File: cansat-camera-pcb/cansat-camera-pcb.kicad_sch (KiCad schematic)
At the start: 25 parts, among them SW2 SW_Push, U4 STM32H743ZITx, Y1 24MHz

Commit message: USB fix
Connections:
- net usb_dm: now reaches U4.75 (PB14)
- net usb_dp: now reaches U4.76 (PB15)
- no-connect marks 45 -> 43
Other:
- sheet Connector section ports: added USB_DM, USB_DP; removed none
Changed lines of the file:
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@@
 	)
 	(no_connect
-		(at 123.19 148.59)
-	)
-	(no_connect
 		(at 123.19 123.19)
 	)
@@
 	)
 	(no_connect
-		(at 123.19 151.13)
-	)
-	(no_connect
 		(at 57.15 128.27)
 	)
@@
 	(wire
 		(pts
+			(xy 157.48 212.09) (xy 158.75 212.09)
+		)
+		(stroke
+			(width 0)
+			(type default)
+		)
+	)
+	(wire
+		(pts
 			(xy 74.93 57.15) (xy 77.47 57.15)
 		)
@@
 	(wire
 		(pts
+			(xy 157.48 207.01) (xy 158.75 207.01)
+		)
+		(stroke
+			(width 0)
+			(type default)
+		)
+	)
+	(wire
+		(pts
 			(xy 45.72 226.06) (xy 46.99 226.06)
 		)
@@
 	(wire
 		(pts
+			(xy 157.48 209.55) (xy 158.75 209.55)
+		)
+		(stroke
+			(width 0)
+			(type default)
+		)
+	)
+	(wire
+		(pts
 			(xy 43.18 260.35) (xy 53.34 260.35)
 		)
@@
 	(wire
 		(pts
-			(xy 157.48 209.55) (xy 158.75 209.55)
-		)
-		(stroke
-			(width 0)
-			(type default)
-		)
-	)
-	(wire
-		(pts
 			(xy 158.75 135.89) (xy 160.02 135.89)
 		)
@@
 	(wire
 		(pts
-			(xy 157.48 207.01) (xy 158.75 207.01)
+			(xy 157.48 204.47) (xy 158.75 204.47)
 		)
 		(stroke
@@
 		)
 	)
+	(label "usb_dm"
+		(at 157.48 212.09 180)
+		(effects
+			(font
+				(size 1.27 1.27)
+			)
+			(justify right bottom)
+		)
+	)
 	(label "VREF_PIN"
 		(at 55.88 80.01 180)
@@
 		)
 	)
+	(label "usb_dp"
+		(at 157.48 209.55 180)
+		(effects
+			(font
+				(size 1.27 1.27)
+			)
+			(justify right bottom)
+		)
+	)
+	(label "usb_dp"
+		(at 123.19 151.13 0)
+		(effects
+			(font
+				(size 1.27 1.27)
+			)
+			(justify left bottom)
+		)
+	)
 	(label "FMC_SDCKE0"
 		(at 124.46 163.83 0)
@@
 	)
 	(label "UART4_RX"
-		(at 157.48 209.55 180)
+		(at 157.48 207.01 180)
 		(effects
 			(font
@@
 		)
 	)
+	(label "usb_dm"
+		(at 123.19 148.59 0)
+		(effects
+			(font
+				(size 1.27 1.27)
+			)
+			(justify left bottom)
+		)
+	)
 	(label "FMC_D3"
 		(at 158.75 53.34 180)
@@
 	)
 	(label "UART4_TX"
-		(at 157.48 207.01 180)
+		(at 157.48 204.47 180)
 		(effects
 			(font
@@
 			)
 		)
-		(pin "OBC_UART_Rx" input
-			(at 158.75 209.55 180)
-			(effects
-				(font
-					(size 1.27 1.27)
-				)
-				(justify left)
-			)
-		)
 		(pin "BOOT0" input
 			(at 190.5 205.74 0)
@@
 		)
 		(pin "OBC_UART_Tx" output
+			(at 158.75 204.47 180)
+			(effects
+				(font
+					(size 1.27 1.27)
+				)
+				(justify left)
+			)
+		)
+		(pin "USB_DP" bidirectional
+			(at 158.75 209.55 180)
+			(effects
+				(font
+					(size 1.27 1.27)
+				)
+				(justify left)
+			)
+		)
+		(pin "USB_DM" bidirectional
+			(at 158.75 212.09 180)
+			(effects
+				(font
+					(size 1.27 1.27)
+				)
+				(justify left)
+			)
+		)
+		(pin "OBC_UART_Rx" input
 			(at 158.75 207.01 180)
 			(effects

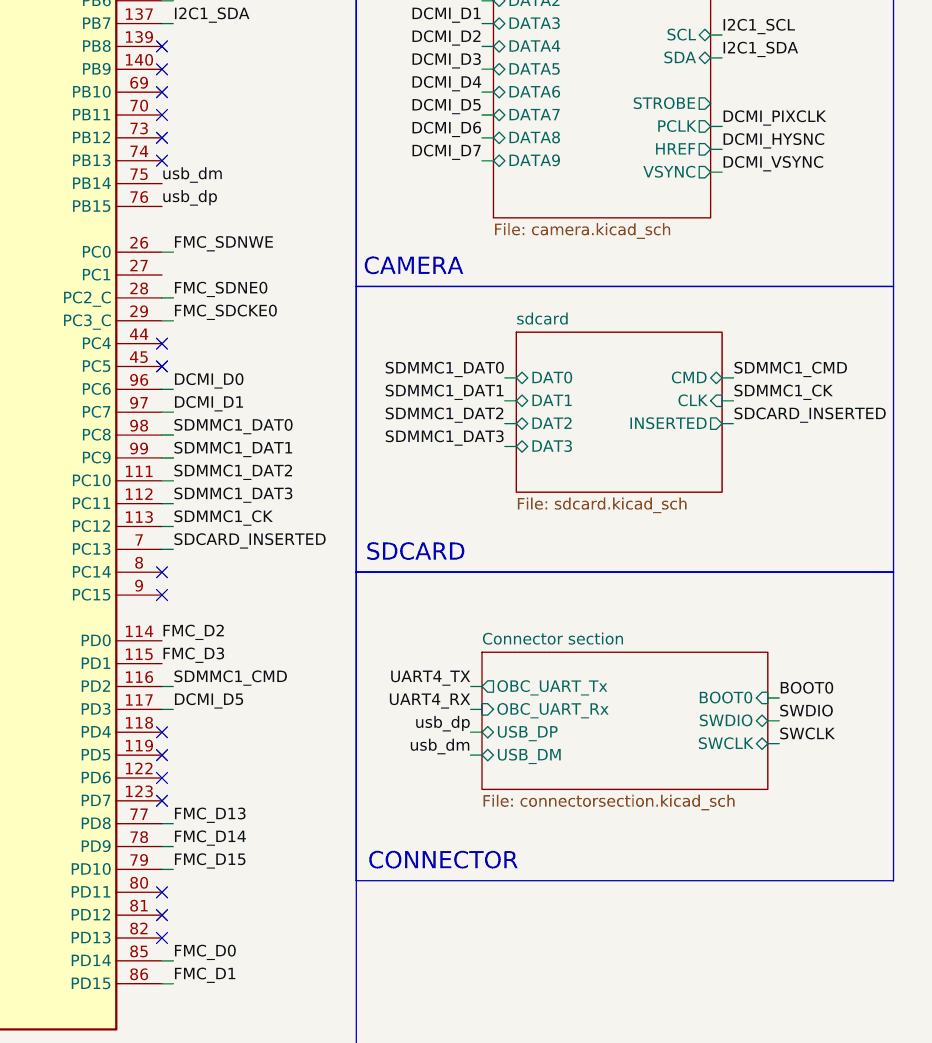
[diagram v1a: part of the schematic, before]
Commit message: sdcard deleted form this PCB
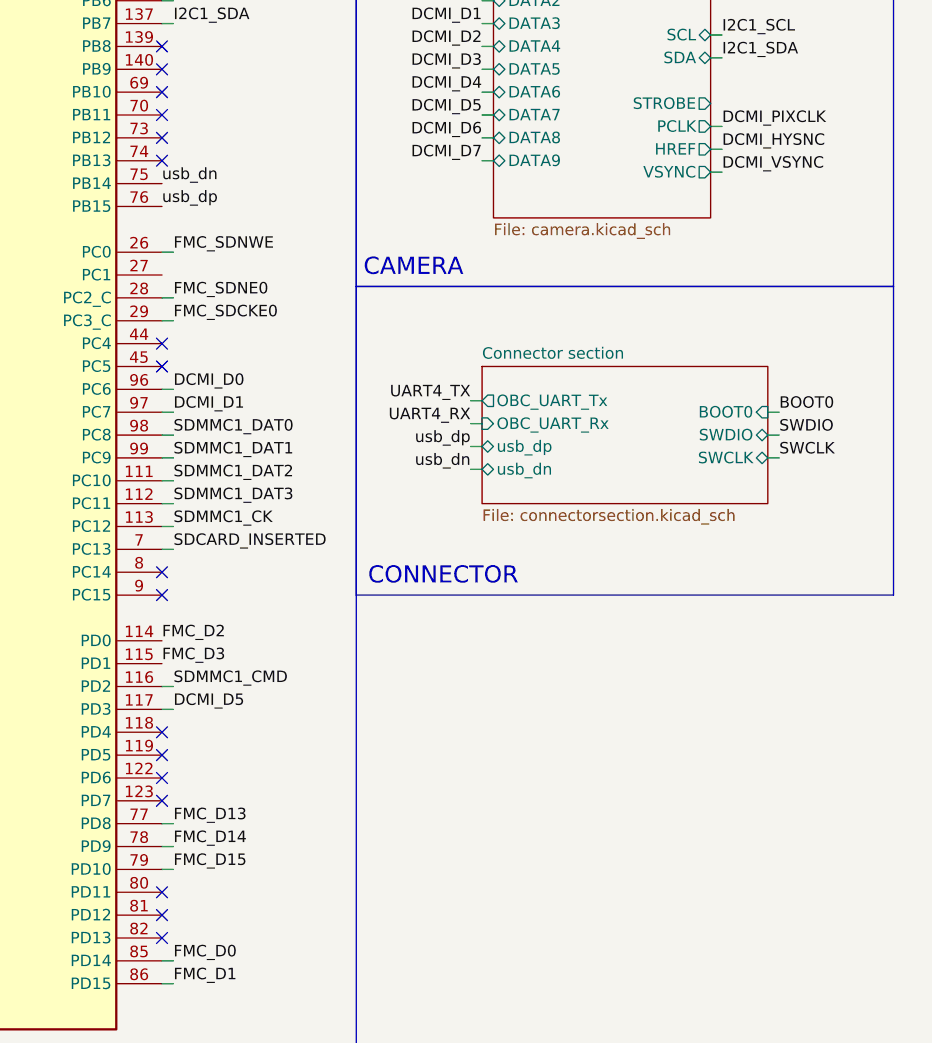
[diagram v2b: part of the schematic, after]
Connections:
- net usb_dm renamed usb_dn
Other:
- removed sheet sdcard
- sheet Connector section ports: added usb_dn, usb_dp; removed USB_DM, USB_DP
- note removed: "SDCARD"

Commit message: -
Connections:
- net usb_dn renamed usb_DN
- net usb_dp renamed usb_DP
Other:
- sheet Connector section ports: added usb_DN, usb_DP; removed usb_dn, usb_dp
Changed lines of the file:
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@@
 		)
 	)
-	(label "usb_dn"
+	(label "usb_DN"
 		(at 157.48 180.34 180)
 		(effects
@@
 		)
 	)
-	(label "usb_dp"
+	(label "usb_DP"
 		(at 157.48 177.8 180)
 		(effects
@@
 		)
 	)
-	(label "usb_dp"
+	(label "usb_DP"
 		(at 123.19 151.13 0)
 		(effects
@@
 		)
 	)
-	(label "usb_dn"
+	(label "usb_DN"
 		(at 123.19 148.59 0)
 		(effects
@@
 			)
 		)
-		(pin "usb_dn" bidirectional
+		(pin "usb_DN" bidirectional
 			(at 158.75 180.34 180)
 			(effects
@@
 			)
 		)
-		(pin "usb_dp" bidirectional
+		(pin "usb_DP" bidirectional
 			(at 158.75 177.8 180)
 			(effects

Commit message: fixes
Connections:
- net LTE_reset: now reaches U4.1 (PE2)
- net LTE_pwrkey: now reaches U4.2 (PE3)
- no-connect marks 43 -> 41
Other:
- sheet Connector section ports: added pwrkey, reset; removed none
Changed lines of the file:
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@@
 	)
 	(no_connect
-		(at 57.15 189.23)
-	)
-	(no_connect
 		(at 57.15 115.57)
 	)
@@
 	)
 	(no_connect
-		(at 57.15 191.77)
-	)
-	(no_connect
 		(at 123.19 125.73)
 	)
@@
 	(wire
 		(pts
-			(xy 191.77 173.99) (xy 190.5 173.99)
+			(xy 191.77 171.45) (xy 190.5 171.45)
 		)
 		(stroke
@@
 	(wire
 		(pts
-			(xy 190.5 176.53) (xy 191.77 176.53)
+			(xy 190.5 173.99) (xy 191.77 173.99)
 		)
 		(stroke
@@
 	(wire
 		(pts
+			(xy 55.88 191.77) (xy 57.15 191.77)
+		)
+		(stroke
+			(width 0)
+			(type default)
+		)
+	)
+	(wire
+		(pts
 			(xy 55.88 219.71) (xy 57.15 219.71)
 		)
@@
 	(wire
 		(pts
-			(xy 190.5 179.07) (xy 191.77 179.07)
+			(xy 55.88 189.23) (xy 57.15 189.23)
+		)
+		(stroke
+			(width 0)
+			(type default)
+		)
+	)
+	(wire
+		(pts
+			(xy 190.5 176.53) (xy 191.77 176.53)
 		)
 		(stroke
@@
 	(wire
 		(pts
+			(xy 190.5 179.07) (xy 191.77 179.07)
+		)
+		(stroke
+			(width 0)
+			(type default)
+		)
+	)
+	(wire
+		(pts
 			(xy 184.15 99.06) (xy 185.42 99.06)
 		)
@@
 	(wire
 		(pts
+			(xy 190.5 181.61) (xy 191.77 181.61)
+		)
+		(stroke
+			(width 0)
+			(type default)
+		)
+	)
+	(wire
+		(pts
 			(xy 49.53 67.31) (xy 46.99 67.31)
 		)
@@
 		)
 	)
+	(label "LTE_reset"
+		(at 191.77 179.07 0)
+		(effects
+			(font
+				(size 1.27 1.27)
+			)
+			(justify left bottom)
+		)
+	)
 	(label "VREF_PIN"
 		(at 55.88 80.01 180)
@@
 		)
 	)
+	(label "LTE_pwrkey"
+		(at 55.88 191.77 180)
+		(effects
+			(font
+				(size 1.27 1.27)
+			)
+			(justify right bottom)
+		)
+	)
 	(label "FMC_A6"
 		(at 55.88 171.45 180)
@@
 	)
 	(label "BOOT0"
-		(at 191.77 173.99 0)
+		(at 191.77 171.45 0)
 		(effects
 			(font
@@
 		)
 	)
+	(label "LTE_pwrkey"
+		(at 191.77 181.61 0)
+		(effects
+			(font
+				(size 1.27 1.27)
+			)
+			(justify left bottom)
+		)
+	)
 	(label "VDDA_PIN"
 		(at 107.95 55.88 90)
@@
 	)
 	(label "SWCLK"
-		(at 191.77 179.07 0)
+		(at 191.77 176.53 0)
 		(effects
 			(font
@@
 		)
 	)
+	(label "LTE_reset"
+		(at 55.88 189.23 180)
+		(effects
+			(font
+				(size 1.27 1.27)
+			)
+			(justify right bottom)
+		)
+	)
 	(label "SWDIO"
-		(at 191.77 176.53 0)
+		(at 191.77 173.99 0)
 		(effects
 			(font
@@
 		)
 		(pin "BOOT0" input
-			(at 190.5 173.99 0)
+			(at 190.5 171.45 0)
 			(effects
 				(font
@@
 		)
 		(pin "SWDIO" bidirectional
-			(at 190.5 176.53 0)
+			(at 190.5 173.99 0)
 			(effects
 				(font
@@
 		)
 		(pin "SWCLK" bidirectional
-			(at 190.5 179.07 0)
+			(at 190.5 176.53 0)
 			(effects
 				(font
@@
 			)
 		)
+		(pin "reset" output
+			(at 190.5 179.07 0)
+			(effects
+				(font
+					(size 1.27 1.27)
+				)
+				(justify right)
+			)
+		)
+		(pin "pwrkey" output
+			(at 190.5 181.61 0)
+			(effects
+				(font
+					(size 1.27 1.27)
+				)
+				(justify right)
+			)
+		)

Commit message: Sdram finish, cleanup
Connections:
- net FMC_A12: now reaches U4.87 (PG2)
- net FMC_AP: no longer names the net of U4.18 (PF6)
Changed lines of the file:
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@@
 	)
 	(no_connect
-		(at 57.15 102.87)
-	)
-	(no_connect
 		(at 123.19 82.55)
 	)
@@
 	)
 	(no_connect
+		(at 57.15 156.21)
+	)
+	(no_connect
 		(at 123.19 191.77)
 	)
@@
 	(wire
 		(pts
+			(xy 55.88 102.87) (xy 57.15 102.87)
+		)
+		(stroke
+			(width 0)
+			(type default)
+		)
+	)
+	(wire
+		(pts
 			(xy 39.37 228.6) (xy 39.37 231.14)
 		)
@@
 		)
 	)
+	(label "FMC_A12"
+		(at 55.88 102.87 180)
+		(effects
+			(font
+				(size 1.27 1.27)
+			)
+			(justify right bottom)
+		)
+	)
 	(label "USART2_TX"
 		(at 124.46 74.93 0)
@@
 		)
 	)
-	(label "FMC_A10"
+	(label "FMC_A11"
 		(at 185.42 73.66 0)
 		(effects
@@
 		)
 	)
-	(label "FMC_AP"
+	(label "FMC_A10"
 		(at 185.42 71.12 0)
 		(effects
@@
 		)
 	)
-	(label "FMC_A11"
+	(label "FMC_A12"
 		(at 185.42 76.2 0)
 		(effects
@@
 		)
 	)
-	(label "FMC_AP"
-		(at 57.15 156.21 180)
-		(effects
-			(font
-				(size 1.27 1.27)
-			)
-			(justify right bottom)
-		)
-	)

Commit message: Camera_Final
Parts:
- removed Y1: 24MHz, Crystal:Crystal_SMD_3225-4Pin_3.2x2.5mm, symbol Device:Crystal_Small
- added Y1: 24MHz, Crystal:Crystal_SMD_3225-4Pin_3.2x2.5mm, symbol Device:Crystal_GND24_Small
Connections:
- net GND: now also Y1.2, Y1.4
- net at C1.1, U4.23 (PH0): now also Y1.3
- net at C34.2, U4.24 (PH1): now also Y1.1
- net I2C2_SCL: now reaches U4.69 (PB10)
- net I2C2_SDA: now reaches U4.70 (PB11)
- net I2C4_SCL: now reaches U4.81 (PD12)
- net I2C4_SDA: now reaches U4.82 (PD13)
- net SDCARD_INSERTED: no longer names the net of U4.7 (PC13)
- net SDMMC1_CK: no longer names the net of U4.113 (PC12)
- net SDMMC1_DAT0: no longer names the net of U4.98 (PC8)
- net SDMMC1_DAT1: no longer names the net of U4.99 (PC9)
- net SDMMC1_DAT2: no longer names the net of U4.111 (PC10)
- net SDMMC1_DAT3: no longer names the net of U4.112 (PC11)
- no-connect marks 41 -> 44
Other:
- added sheet sz4pF4SZ (extraf4sz.kicad_sch)
- sheet Connector section ports: added I2C2_SCL, I2C2_SDA, I2C4_SCL, I2C4_SDA; removed none
- note added: "Extra"

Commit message: Camera_Final
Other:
- removed sheet sz4pF4SZ
- note removed: "Extra"
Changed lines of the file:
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@@
 	)
 	(rectangle
-		(start 144.78 194.31)
-		(end 204.47 228.6)
-		(stroke
-			(width 0)
-			(type default)
-		)
-		(fill
-			(type none)
-		)
-	)
-	(rectangle
 		(start 19.05 17.78)
 		(end 144.78 281.94)
@@
 		)
 	)
-	(text "Extra"
-		(exclude_from_sim no)
-		(at 149.098 226.822 0)
-		(effects
-			(font
-				(size 1.905 1.905)
-			)
-		)
-	)
 	(junction
 		(at 100.33 57.15)
@@
 			)
 		)
-		(instances
-			(project "cansat-camera-pcb"
-				(path "/ff55e53a-9379-43eb-9b08-9bace1f81889"
-					(page "6")
-				)
-			)
-		)
-	)
-	(sheet
-		(at 161.29 203.2)
-		(size 21.59 13.97)
-		(exclude_from_sim no)
-		(in_bom yes)
-		(on_board yes)
-		(dnp no)
-		(fields_autoplaced yes)
-		(stroke
-			(width 0.1524)
-			(type solid)
-		)
-		(fill
-			(color 0 0 0 0.0000)
-		)
-		(property "Sheetname" "sz4pF4SZ"
-			(at 161.29 202.4884 0)
-			(effects
-				(font
-					(size 1.27 1.27)
-				)
-				(justify left bottom)
-			)
-		)
-		(property "Sheetfile" "extraf4sz.kicad_sch"
-			(at 161.29 217.7546 0)
-			(effects
-				(font
-					(size 1.27 1.27)
-				)
-				(justify left top)
-			)
-		)

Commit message: some fixes
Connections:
- net I2C2_SCL: no longer names the net of U4.69 (PB10)
- net I2C2_SDA: no longer names the net of U4.70 (PB11)
- net OV5640_XCLK: no longer names the net of U4.102 (PA10)
- net SDMMC1_CMD: no longer names the net of U4.116 (PD2)
- net USART2_RX: no longer names the net of U4.37 (PA3)
- net USART2_TX: no longer names the net of U4.36 (PA2)
- no-connect marks 44 -> 50
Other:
- sheet Connector section ports: added none; removed I2C4_SCL, I2C4_SDA
- sheet camera ports: added none; removed XCLK
